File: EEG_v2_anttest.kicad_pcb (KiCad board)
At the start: 2 copper layers, 66.9 x 41.5 mm, 115 parts, among them P1 CONN_2, P2 CONN_8, P3 USB_A, P4 CONN_8, P5 CONN_5X2, P6 CONN_2, P7 CONN_1, SW1 SWITCH_INV, SW2 RESET, SW3 SW_PUSH_4PIN, SW4 SW_PUSH_4PIN, U1 ADS1299IPAGR, U2 TLV70033, U3 TLV70025, U4 LM2664, U5 TPS72325, U6 CC2540, U7 2450BM15A0002E, X1 QUARTZCMS4_32K, X2 QUARTZCMS4_MOD

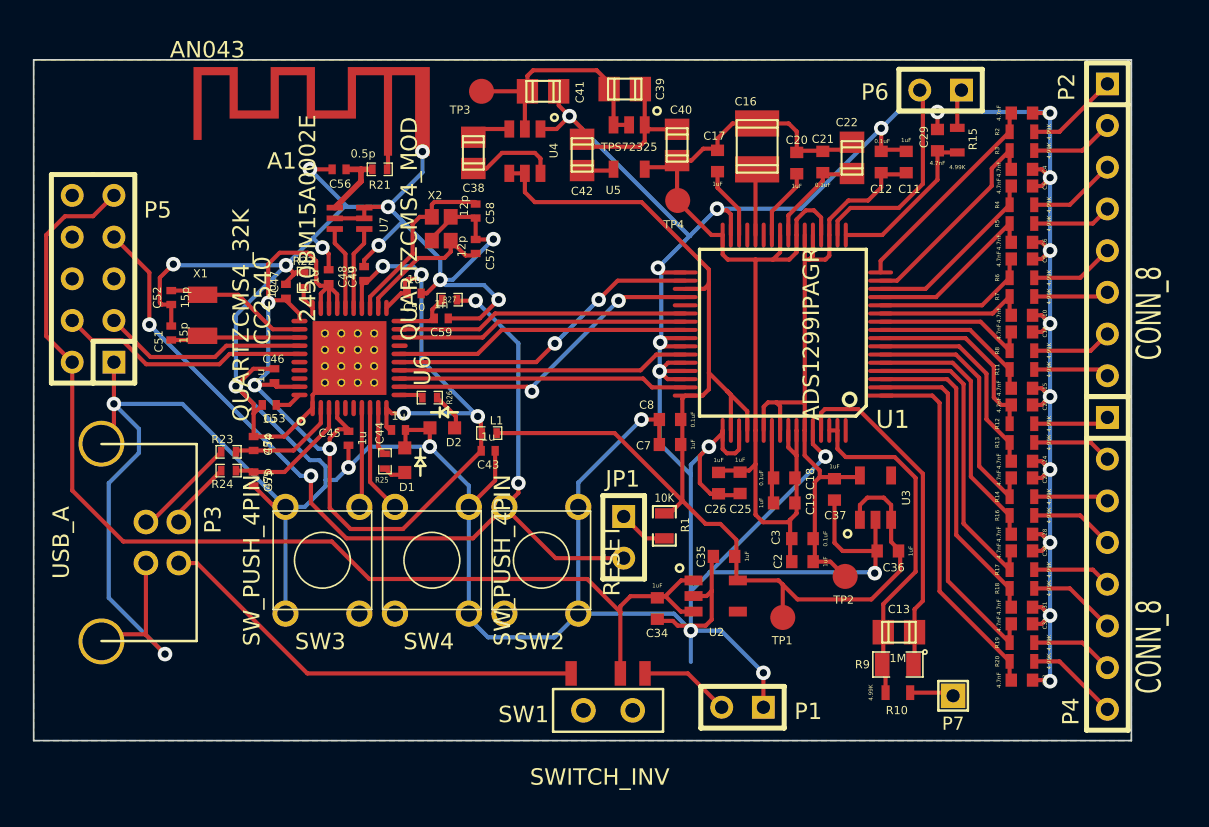
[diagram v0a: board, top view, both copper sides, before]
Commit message: Continue layout, test antenna workings
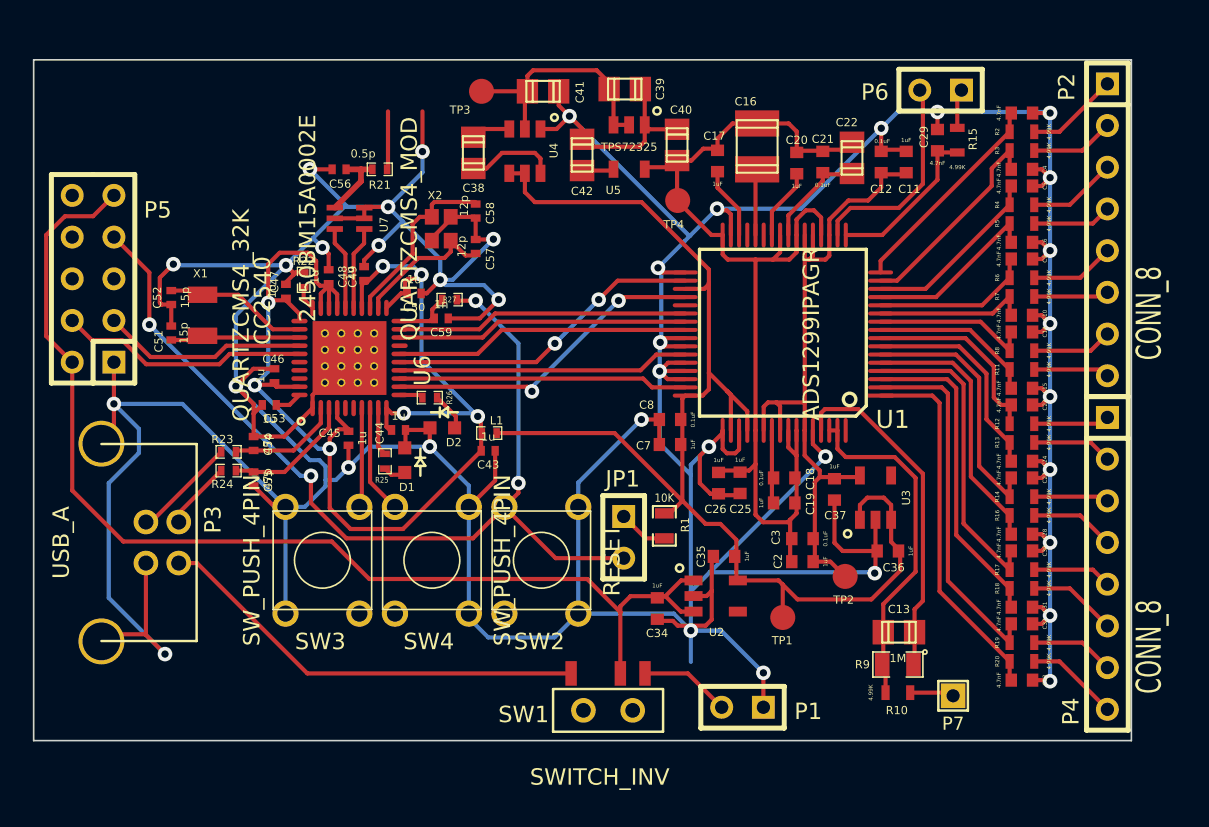
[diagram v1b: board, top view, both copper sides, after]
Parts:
- removed A1: AN043, AN043
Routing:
- removed copper zone on B.Cu, net AGND
- removed copper zone on F.Cu, net AGND
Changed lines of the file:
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@@
 (kicad_pcb (version 3) (host pcbnew "(2013-07-07 BZR 4022)-stable")
   (general
-    (links 288)
+    (links 284)
     (no_connects 0)
     (area 257.517999 137.8966 333.18577 184.852)
@@
     (tracks 836)
     (zones 0)
-    (modules 115)
+    (modules 114)
     (nets 88)
   )
@@
     )
   )
-  (module AN043 (layer F.Cu)
-    (at 275.6535 145.923)
-    (clearance -0.1)
-    (fp_text reference A1 (at 3.429 0.5715) (layer F.SilkS)
-      (effects (font (size 1 1) (thickness 0.15)))
-    )
-    (fp_text value AN043 (at -1.1 -6.2) (layer F.SilkS)
-      (effects (font (size 1 1) (thickness 0.15)))
-    )
-    (fp_line (start -2.25 -0.25) (end -2.25 -5.45) (layer Dwgs.User) (width 0.001))
-    (fp_line (start 12.95 -5.45) (end 12.95 -0.25) (layer Dwgs.User) (width 0.001))
-    (fp_line (start 12.95 -0.25) (end -2.25 -0.25) (layer Dwgs.User) (width 0.001))
-    (fp_line (start 12.45 -5.45) (end 12.95 -5.45) (layer Dwgs.User) (width 0.001))
-    (fp_line (start -1.65 -5.45) (end -2.25 -5.45) (layer Dwgs.User) (width 0.001))
-    (fp_line (start 12.45 -5.45) (end -1.65 -5.45) (layer Dwgs.User) (width 0.001))
-    (pad 1 smd rect (at 9.9 0 180) (size 0.5 0.5)
-      (layers F.Cu F.Paste F.Mask)
-      (net 37 /Microcontroller/ANTENNA)
-    )
-    (pad 1 smd rect (at 9.9 -2.45 180) (size 0.5 4.4)
-      (layers F.Cu F.Paste F.Mask)
-      (net 37 /Microcontroller/ANTENNA)
-    )
-    (pad 2 smd rect (at 12 0 180) (size 0.9 0.5)
-      (layers F.Cu F.Paste F.Mask)
-      (net 61 AGND)
-    )
-    (pad 2 smd rect (at 12 -2.45 180) (size 0.9 4.4)
-      (layers F.Cu F.Paste F.Mask)
-      (net 61 AGND)
-    )
-    (pad "" smd rect (at 9.95 -4.9 180) (size 5 0.5)
-      (layers F.Cu F.Paste F.Mask)
-    )
-    (pad "" smd rect (at 7.7 -3.33 180) (size 0.5 2.64)
-      (layers F.Cu F.Paste F.Mask)
-    )
-    (pad "" smd rect (at 6.45 -2.26 180) (size 2 0.5)
-      (layers F.Cu F.Paste F.Mask)
-    )
-    (pad "" smd rect (at 5.2 -3.33 180) (size 0.5 2.64)
-      (layers F.Cu F.Paste F.Mask)
-    )
-    (pad "" smd rect (at 3 -3.33 180) (size 0.5 2.64)
-      (layers F.Cu F.Paste F.Mask)
-    )
-    (pad "" smd rect (at 0.5 -3.33 180) (size 0.5 2.64)
-      (layers F.Cu F.Paste F.Mask)
-    )
-    (pad "" smd rect (at 4.1 -4.9 180) (size 2.7 0.5)
-      (layers F.Cu F.Paste F.Mask)
-    )
-    (pad "" smd rect (at -0.6 -4.9 180) (size 2.7 0.5)
-      (layers F.Cu F.Paste F.Mask)
-    )
-    (pad "" smd rect (at 1.75 -2.26 180) (size 2 0.5)
-      (layers F.Cu F.Paste F.Mask)
-    )
-    (pad "" smd rect (at -1.7 -2.68 180) (size 0.5 3.94)
-      (layers F.Cu F.Paste F.Mask)
-    )
-  )
   (module Everlight_LED (layer F.Cu)
     (at 286.5755 164.719 270)
@@
   (segment (start 280.6425 177.709) (end 296.708 177.709) (width 0.254) (layer F.Cu) (net 60))
   (segment (start 273.919 170.9855) (end 280.6425 177.709) (width 0.254) (layer F.Cu) (net 60))
-  (segment (start 295.9525 142.25) (end 295.9525 143.108) (width 0.254) (layer F.Cu) (net 61) (status 400000))
+  (segment (start 295.9525 142.25) (end 295.9525 143.108) (width 0.254) (layer F.Cu) (net 61))
   (segment (start 295.9525 143.108) (end 296.6085 143.764) (width 0.254) (layer F.Cu) (net 61))
-  (segment (start 297.375 145.1725) (end 297.375 144.5305) (width 0.254) (layer F.Cu) (net 61) (status C00000))
-  (segment (start 297.375 144.5305) (end 296.6085 143.764) (width 0.254) (layer F.Cu) (net 61) (status 400000))
-  (segment (start 294.8415 144.5455) (end 295.827 144.5455) (width 0.254) (layer F.Cu) (net 61) (status 400000))
+  (segment (start 297.375 145.1725) (end 297.375 144.5305) (width 0.254) (layer F.Cu) (net 61))
+  (segment (start 297.375 144.5305) (end 296.6085 143.764) (width 0.254) (layer F.Cu) (net 61))
+  (segment (start 294.8415 144.5455) (end 295.827 144.5455) (width 0.254) (layer F.Cu) (net 61))
   (segment (start 295.827 144.5455) (end 296.6085 143.764) (width 0.254) (layer F.Cu) (net 61))
   (segment (start 303.8905 151.046) (end 303.954 151.046) (width 0.254) (layer B.Cu) (net 61))
@@
       )
     )
-  )
-  (zone (net 61) (net_name AGND) (layer B.Cu) (hatch edge 0.508)
-    (connect_pads yes (clearance 0.254))
-    (min_thickness 0.254)
-    (fill (arc_segments 16) (thermal_gap 0.508) (thermal_bridge_width 0.508))
-    (polygon
-      (pts
-        (xy 330.835 140.335) (xy 263.9695 140.335) (xy 263.9695 181.8005) (xy 330.835 181.8005)
-      )
-    )
-  )
-  (zone (net 61) (net_name AGND) (layer F.Cu) (hatch edge 0.508)
-    (connect_pads yes (clearance 0.254))
-    (min_thickness 0.254)
-    (fill (arc_segments 16) (thermal_gap 0.508) (thermal_bridge_width 0.508))
-    (polygon
-      (pts
-        (xy 263.9695 140.335) (xy 263.9695 181.8005) (xy 330.835 181.8005) (xy 330.835 140.335)
-      )
-    )
